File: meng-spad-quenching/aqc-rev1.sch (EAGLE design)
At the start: 56 parts, among them IC1 ADCMP582, IC2 NC7SV74K8X, IC3 LT3032-5, J1 VIN_LOGIC, U1 SN65EPT21DGK, U2 TPS78233DDCT, U3 SN65EPT22DGK, X1 CONN_SPAD, X2 CONN_SCOPE_COMP, X3 CONN_SCOPE_RSHUNT, X4 CONN_VA_BIAS, X5 CONN_LATCH_IN

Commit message: Added Peregrine gate drive IC, added one-shot to aqc
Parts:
- added C20: 1n, rcl:C-EUC0603
- added C21, C24: 10n, rcl:C-EUC0603
- added C25: 100n, rcl:C-EUC0603
- added IC4: PE29100, meng:PE29100
- added M1: BSS806N, meng:BSS806N
- added M2, M3: EPC2040, meng:EPC2040
- added R16: DNP, rcl:R-EU_R0603
- added RT2: 3269W-1-101LF, meng:BOURNS_3269WX
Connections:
- removed net N$5: IC2.!PRE, IC2.D, IC2.VDD
- new net !LOGIC_QUENCH: IC2.!Q, M1.G
- new net LOGIC_QUENCH: IC2.Q, R16.2, RT2.1
- new net N$11: M3.D
- new net N$13: M2.S
- new net N$14: M2.G
- new net N$15: M3.G
- new net N$7: C20.1, IC2.!CLR, M1.D, R16.1, RT2.2, RT2.3
- net GND: now also C20.2, C21.2, C24.2, C25.2, M1.S
- net PP_P3V3: now also C24.1, C25.1, IC2.!PRE, IC2.D, IC2.VDD
- net VREF: now also C21.1
- net VSPAD: now also M2.D, M3.S
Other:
- note added: "One-Shot (Holdoff Time)"
- moved on the sheet: C10, C11, C12, C13, C14, C15, C16, C17, C18, C19, C22, C23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

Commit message: No significant changes
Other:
- note added: "HIGH = Latch Disabled"
- note added: "LOW = Latch Enabled"
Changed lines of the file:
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@@
 <text x="243.84" y="208.28" size="1.778" layer="98">One-Shot (Holdoff Time)</text>
 <text x="297.18" y="167.64" size="1.778" layer="98">100R</text>
+<text x="266.7" y="63.5" size="1.778" layer="98">HIGH = Latch Disabled</text>
+<text x="266.7" y="60.96" size="1.778" layer="98">LOW = Latch Enabled</text>
 </plain>
 <instances>

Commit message: Work on AQC rev. 1
Added buffer
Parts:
- removed M2, M3: EPC2040, meng:EPC2040
- added C26, C27, C29, C31: 10n, rcl:C-EUC0603
- added C28, C30, C32: 100n, rcl:C-EUC0603
- added C33: 33u, 25V, rcl:CPOL-EUCT7343
- added IC5: OPA342, meng:OPA333DBV
- added Q1, Q2, Q3, Q4, Q5: MMBTH81, transistor-pnp:MMBTH81LT1SMD
- added R17, R18, R19, R20, R21: 49R9, rcl:R-EU_R0603
- added R22: 100R, rcl:R-EU_R0603
- added R23, R24, R25, R26: 1k, rcl:R-EU_R0603
- added R27: 470R, rcl:R-EU_R0603
- added R28: 1k43, rcl:R-EU_R0603
- added R29: 47R, rcl:R-EU_R0603
- added T1, T2, T3, T4, T5, T6, T7: MMBTH10, transistor:MMBTH10LT1-NPN-SOT23-BEC
- C1: value 33p -> 100n; device rcl:C-EUC0805 -> rcl:C-EUC0603
- IC4: value PE29100 -> OPA342; device meng:PE29100 -> meng:OPA333DBV
- R1: value 65k -> 470R; device rcl:R-EU_R0805 -> rcl:R-EU_R0603
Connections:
- new net DAC_CASCODE_IBIAS: IC5.+IN
- new net DAC_DIAMOND_IBIAS: IC4.+IN
- new net LOGIC_QUENCH_ATTEN: T6.B
- new net N$12: C26.1, Q3.C, R18.2, T2.B
- new net N$16: IC4.OUT, T3.B, T4.B
- new net N$18: Q4.C, Q5.B, R28.2
- new net N$19: C26.2, Q1.B, R20.1, T3.C
- new net N$20: R23.2, T3.E
- new net N$21: Q2.B, R21.1, T1.B
- new net N$22: R1.1, R21.2, T5.C
- new net N$23: IC4.-IN, R24.2, T4.E
- new net N$24: R27.2, T6.E, T7.C
- new net N$26: Q3.E, R25.1
- new net N$27: R28.1, T4.C
- new net N$29: Q4.E, R26.1
- new net N$30: IC5.OUT, T7.B
- new net N$31: Q3.B, Q4.B, Q5.E
- new net N$5: R17.2, T2.E
- new net PP_P15V0: C31.1, C32.1, C33.+, R1.2, R25.2, R26.2, T1.C, T2.C
- new net SPAD_PULLDN_SENSE: Q1.C, R22.2
- net GND: now also C1.2, C27.2, C28.2, C29.2, C30.2, C31.2, C32.2, C33.-, IC4.V-, IC5.V+, Q2.C, Q5.C, R22.1, R23.1, R24.1
- net N$11: now also Q2.E, R18.1; no longer M3.D
- net N$13: now also R20.2, T1.E; no longer M2.S
- net N$14: now also Q1.E, R19.1; no longer M2.G
- net N$15: now also T5.E, T6.C; no longer M3.G
- net PP_N5V0: now also C29.1, C30.1, IC5.-IN, IC5.V-, R27.1, R29.1, R29.2, T7.E
- net PP_P5V0: now also C1.1, C27.1, C28.1, IC4.V+, T5.B
- net VA_FILT: no longer R1.2
- net VCOMP_IN: no longer C1.2
- net VSPAD: now also R17.1, R19.2; no longer C1.1, M2.D, M3.S, R1.1
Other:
- note added: "-0.6V"
- note added: "-4.7V"
- note added: "0.1V"
- note added: "0V"
- note added: "1.6V"
- note added: "10V/V offset"
- note added: "11.35V"
- note added: "12.65V"
- note added: "12.8V"
- note added: "12V"
- note added: "13.4V"
- note added: "14V"
- note added: "15V"
- note added: "1V"
- note added: "1mA/V"
- note added: "5V0 is lower noise than 3V3"
- note added: "All collector currents approx. 1mA"
- note added: "Higher cascode bias = lower Cmu of CE stage"
- note removed: "External cap."
- note removed: "Passive Quench Resistor"
- moved on the sheet: C1, R1, X1

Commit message: Added LTC1711, upated one-shot design
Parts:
- removed C3: 33u, 25V, rcl:CPOL-EUCT7343
- removed C4, C5: 10u, rcl:C-EUC1206
- removed R13: 50R, rcl:R-EU_R0603
- removed RT2: 3269W-1-101LF, meng:BOURNS_3269WX
- removed X4: CONN_VA_BIAS, con-coax:SMA-142-0711-871/876
- removed X5: CONN_LATCH_IN, con-coax:SMA-142-0711-871/876
- added C34, C41, C42: 10n, rcl:C-EUC0603
- added C35, C36: 100n, rcl:C-EUC0603
- added C37, C38, C39, C40: 10u, rcl:C-EUC1206
- added IC6: LTC1711, meng:LTC1711
- added IC7: DS1100LU-20+, meng:DS1100L
- added IC8: LT3032-15, meng:LT3032
- added R30: 100R, rcl:R-EU_R0603
- added R31: 10k, rcl:R-EU_R0603
- added R32, R33: DNP, rcl:R-EU_R0603
- added TP5, TP6: TPTP20R, testpad:TPTP20R
- C2: value 100n -> 10n; device rcl:C-EUC0805 -> rcl:C-EUC0603
- R15: value 0R -> DNP
- R16: value DNP -> 470R
- R5: value 50R -> DNP; device rcl:R-EU_R0805 -> rcl:R-EU_R0603
- R7: value 470R -> 1k
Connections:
- net N$1 renamed HOLDOFF_TRIG
- removed net !LOGIC_QUENCH: IC2.!Q, M1.G
- removed net N$10: R13.1, U3.D0, X5G1.1
- removed net VA_FILT: C2.1, C3.+, R5.1
- removed net VA_IN: R5.2, X4G1.1
- removed net VCOMP_IN: IC1.VN, R2.2, R4.1
- removed net VREF: C21.1, IC1.VP, R14.1, R7.2, RT1.2, RT1.3
- new net !ONE_SHOT_CLR: IC2.!CLR, IC6.!Q
- new net BLANKING_LATCH_EN: R12.1, R2.1, R32.1, R33.1, R5.1, U3.D0
- new net N$1: IC7.TAP5, R33.2
- new net N$17: IC7.TAP3, R12.2
- new net N$25: IC6.+IN, R30.1, R31.2
- new net N$28: IC7.TAP2, R5.2
- new net N$32: IC7.TAP1, R2.2
- new net N$33: C42.1, IC8.BP
- new net N$34: C41.1, IC8.BN
- new net N$36: IC3.!SN, IC3.!SP, IC3.IP
- new net NC_!LOGIC_QUENCH: IC2.!Q
- new net ONE_SHOT_CAP: C20.1, M1.D, R16.1, R30.2
- new net ONE_SHOT_CLR: IC6.Q, M1.G, R31.1
- new net ONE_SHOT_VREF: IC6.-IN
- new net PP_N15V0: C40.1, C41.2, IC3.IN, IC3.IN@1, IC8.ON, TP5.TP
- new net VREF_AV_DET: C21.1, IC1.VP, R14.2, R7.1, RT1.1
- net COMP_LE_N: now also U3.Q0; no longer U3.~Q0
- net COMP_LE_P: now also U3.~Q0; no longer U3.Q0
- net GND: now also C34.2, C35.2, C36.2, C37.2, C38.2, C39.2, C40.2, IC6.GND, IC6.LEN, IC6.V-, IC7.GND, IC8.GND, IC8.GND@1, R14.1, RT1.2, RT1.3; no longer C3.-, C4.2, C5.2, R13.2, R14.2, R2.1, RT1.1, X4G1.GND, X5G1.GND
- net LOGIC_QUENCH: now also IC7.IN; no longer RT2.1
- net N$6: no longer R12.2
- net N$7: now also IC7.TAP4, R32.2; no longer C20.1, IC2.!CLR, M1.D, R16.1, RT2.2, RT2.3
- net PP_N5V0: no longer R7.1
- net PP_NVIN: now also C38.1, IC8.IN, IC8.IN@1; no longer C5.1, IC3.IN, IC3.IN@1
- net PP_P15V0: now also C39.1, C42.2, IC8.OP, TP6.TP
- net PP_P3V3: now also C2.1, C34.1, C35.1, C36.1, IC6.V+, IC7.VCC; no longer R12.1
- net PP_P5V0: now also R7.2
- net PP_PVIN: now also C37.1, IC8.!SN, IC8.!SP, IC8.IP; no longer C4.1, IC3.!SN, IC3.!SP, IC3.IP
- net SPAD_PULLDN_SENSE: now also IC1.VN, R4.1
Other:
- note added: "+/- 15V LDO"
- note added: "+50mV Adj."
- note added: "1.0"
- note added: "1/1"
- note added: "1mA"
- note added: "4.4V"
- note added: "4ns per tap, pick lowest tap that provides sufficient recovery blanking"
- note added: "5V"
- note added: "AVALANCHE DETECTOR"
- note added: "Future design can try LTC6752 to reduce BOM cost, in exchange for an extra ~1.5ns of prop. delay"
- note added: "HIGH = Latch Enabled"
- note added: "HOLDOFF ONE-SHOT"
- note added: "LOW = Latch Disabled"
- note added: "Note: I'm not sure why the P/N convention is this way, are pins mixed up?"
- note added: "Note: insufficient recovery blanking = SPAD voltage oscillation"
- note added: "OUTPUT DRIVER"
- note added: "POWER SUPPLIES"
- note added: "Place near input"
- note added: "TABLE OF CONTENTS"
- note removed: "-100mV Adj."
- note removed: "From sig. gen."
- note removed: "HIGH = Latch Disabled"
- note removed: "LOW = Latch Enabled"
- note removed: "One-Shot (Holdoff Time)"
- note removed: "Optional Bias Filter"
- note removed: "Panasonic EEF-CX1E330R"
- note removed: "Use R2 or R4 term. if IC1 not populated"
- note removed: "VA Bias"

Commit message: Started AQC rev. 1 layout, decided to make DACs external
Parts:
- added C3: 100n, rcl:C-EUC0603
- added C4: 10n, rcl:C-EUC0603
- added Q6: MMBTH81, transistor-pnp:MMBTH81LT1SMD
- added R13: 0R, rcl:R-EU_R0603
- added R34, R35, R36, R37, R38, R39, R40, R41, R42, R43, R44, R45, R46: DNP, rcl:R-EU_R0603
- added RT2, RT3, RT4: 3269W-1-102LF, meng:BOURNS_3269WX
- added X4, X5, X6: CONN_VREF_ONE_SHOT_EXT, con-coax:SMA-142-0711-871/876
- R22: value 100R -> 1k
- R29: value 47R -> 470R
- R7: value 1k -> DNP
- RT1: value 3269W-1-101LF -> 3269W-1-102LF
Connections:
- removed net DAC_CASCODE_IBIAS: IC5.+IN
- removed net DAC_DIAMOND_IBIAS: IC4.+IN
- removed net ONE_SHOT_VREF: IC6.-IN
- new net N$10: Q1.C, Q6.E
- new net VREF_CASCODE_IBIAS: IC5.+IN, R43.1, R44.1
- new net VREF_CASCODE_IBIAS_EXT: R43.2, X6G1.1
- new net VREF_CASCODE_IBIAS_INT: R44.2, R45.1, R46.2, RT4.2
- new net VREF_DIAMOND_IBIAS: IC4.+IN, R39.1, R40.1
- new net VREF_DIAMOND_IBIAS_EXT: R39.2, X5G1.1
- new net VREF_DIAMOND_IBIAS_INT: R40.2, R41.1, R42.2, RT3.2
- new net VREF_ONE_SHOT: C4.1, IC6.-IN, R35.1, R36.1
- new net VREF_ONE_SHOT_EXT: R35.2, X4G1.1
- new net VREF_ONE_SHOT_INT: R36.2, R37.1, R38.2, RT2.2
- net GND: now also C3.2, C4.2, R34.2, R37.2, R41.2, R45.2, RT2.3, RT3.3, RT4.3, X4G1.GND, X5G1.GND, X6G1.GND; no longer RT1.2
- net LOGIC_QUENCH: now also R13.2
- net LOGIC_QUENCH_ATTEN: now also R13.1, R34.1
- net PP_P3V3: now also R38.1, R46.1, RT2.1, RT4.1
- net PP_P5V0: now also C3.1, Q6.B, R42.1, RT1.1, RT3.1
- net SPAD_PULLDN_SENSE: now also Q6.C; no longer Q1.C
- net VREF_AV_DET: now also RT1.2; no longer RT1.1
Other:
- note added: "(Expect some offset through the diamond w/. discretes)"
- note added: "1V/V offset"
- note added: "1k"
- note added: "Cascode provides speedup of bias current sensing"
- note added: "For first-time bringup, DNP this CCS:"
- note added: "This reduces V_CE mismatch"
- note added: "by killing Miller cap. of bottom PNP in push-pull"
- note added: "~950mV"
- note removed: "+50mV Adj."
- note removed: "-4.7V"
- note removed: "0.1V"
- note removed: "100R"
- note removed: "10V/V offset"

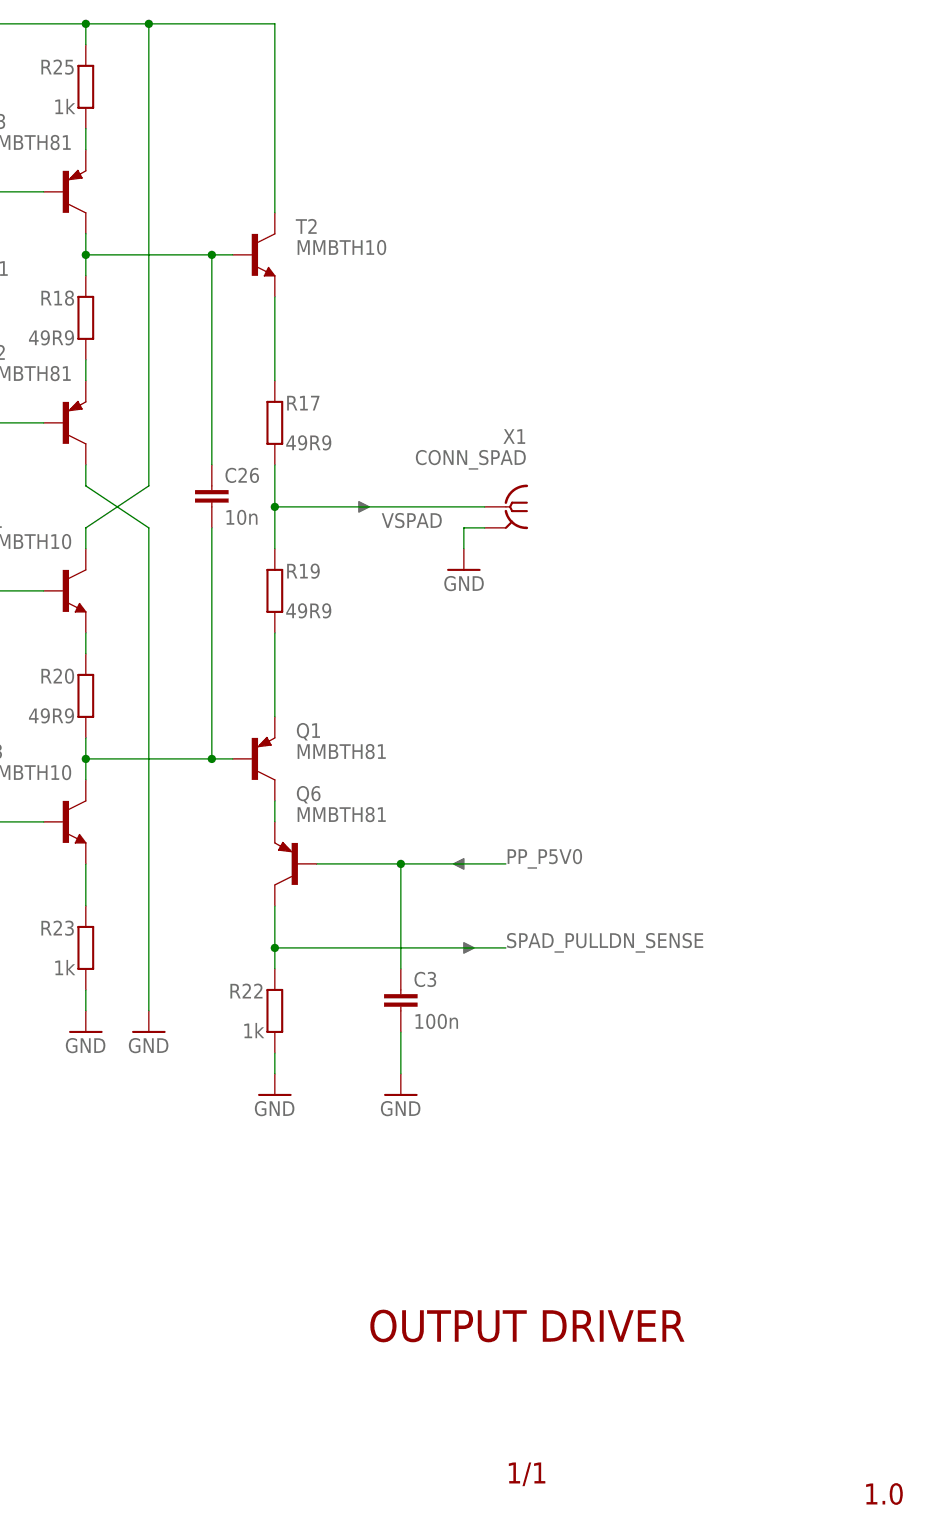
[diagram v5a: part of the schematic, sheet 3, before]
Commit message: Added table of contents, work on AQC layout
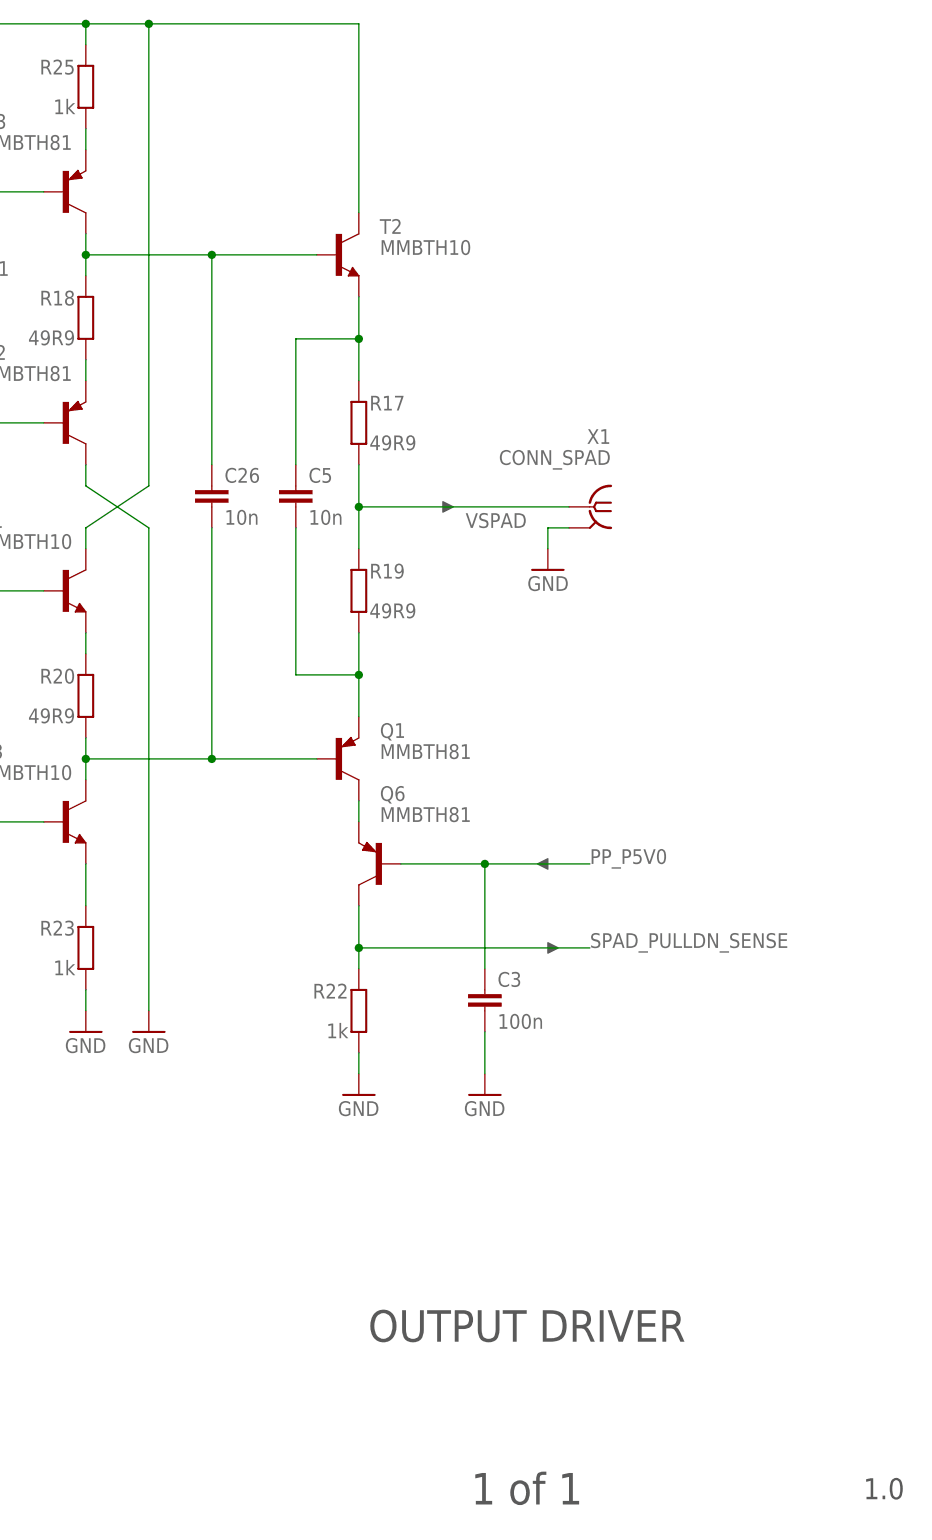
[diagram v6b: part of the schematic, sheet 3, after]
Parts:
- added C5: 10n, rcl:C-EUC0603
- R11: value 50R -> 49R9
- R14, R3, R6, R7: device rcl:R-EU_R0805 -> rcl:R-EU_R0603
- X5: value CONN_VREF_ONE_SHOT_EXT -> CONN_VREF_DIAMOND_IBIAS_EXT
- X6: value CONN_VREF_ONE_SHOT_EXT -> CONN_VREF_CASCODE_IBIAS_EXT
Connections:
- net N$14: now also C5.2
- net N$5: now also C5.1
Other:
- note added: "(T = 1oz/ft^2, H = 9.58mil, Er = 4.6)"
- note added: "1"
- note added: "1 of 1"
- note added: "10mil = 48.5 Ohm SE"
- note added: "2"
- note added: "3"
- note added: "4"
- note added: "5"
- note added: "6"
- note added: "8mil = 52.3 Ohm SE"
- note added: "9mil = 50.3 Ohm SE"
- note added: "CONTENTS"
- note added: "CONTROL INPUT CONNECTORS"
- note added: "Daniel Kramnik"
- note added: "IMPEDANCE CALCULATIONS:"
- note added: "LINEAR ACTIVE SPAD QUENCHING CIRCUIT"
- note added: "Routing Notes:"
- note added: "SHEET"
- note removed: "1/1"
- moved on the sheet: C3, Q1, Q6, R17, R19, R22, T2, X1

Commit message: More routing
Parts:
- removed R6: 49R9, rcl:R-EU_R0603
- removed X3: CONN_SCOPE_RSHUNT, con-coax:SMA-142-0711-871/876
- added C43: 10n, rcl:C-EUC0603
- added C44: 100n, rcl:C-EUC0603
- added IC9: NC7WZ16P6X, meng:NC7WZ16P6X
- added TP4: TPTP20R, testpad:TPTP20R
- R4: value DNP -> 49R9
- X2: value CONN_SCOPE_COMP -> CONN_PHOTON_COUNTER
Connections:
- removed net N$36: IC3.!SN, IC3.!SP, IC3.IP
- removed net VSCOPE_1: R4.2, X3G1.1
- new net N$35: IC5.-IN, R29.2, T7.E
- new net N$37: IC9.OUT1, IC9.OUT2, R4.2
- net GND: now also C43.2, C44.2, IC9.GND; no longer X3G1.GND
- net HOLDOFF_TRIG: no longer R6.2
- net LOGIC_QUENCH: now also IC9.IN1, IC9.IN2
- net N$2: now also R4.1; no longer R6.1
- net PP_N5V0: no longer IC5.-IN, R29.2, T7.E
- net PP_P15V0: now also IC3.!SN, IC3.!SP, IC3.IP
- net PP_P3V3: now also C43.1, C44.1, IC9.VCC, TP4.TP
- net SPAD_PULLDN_SENSE: no longer R4.1
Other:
- note added: "To pulse counter"
- note removed: "To scope"
- moved on the sheet: C10, C11, C37, C38, C39, C40, C41, C42, C6, C7, C8, C9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
